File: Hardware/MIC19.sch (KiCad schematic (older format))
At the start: 14 parts, among them J001 ENGINE_VEL, J002 ENGINE_ACEL, J003 MPPT_POT, J004 SW_PUMP1_ON, J005 SW_PUMP2_ON, J006 SW_PUMP3_ON, J007 SW_BOAT_ON, J008 SW_ENGINE_ON, J009 SW_MPPT_ON, J010 SW_DMS

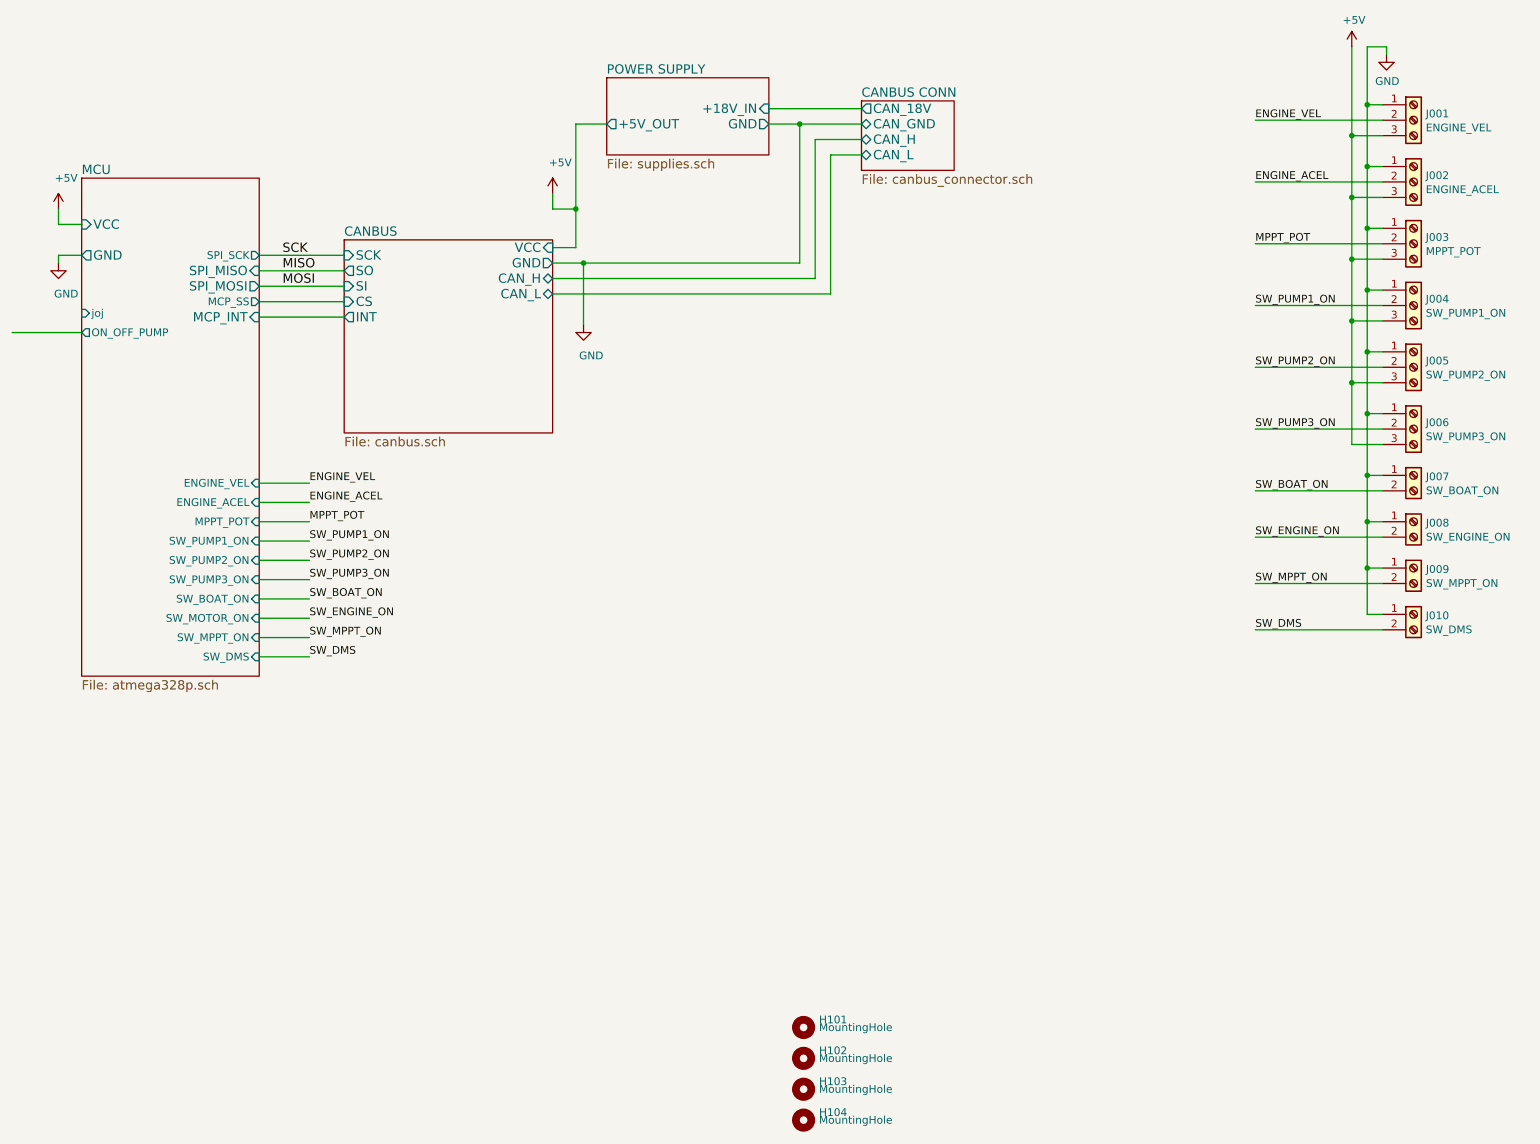
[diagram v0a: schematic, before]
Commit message: Atualização do MIC19
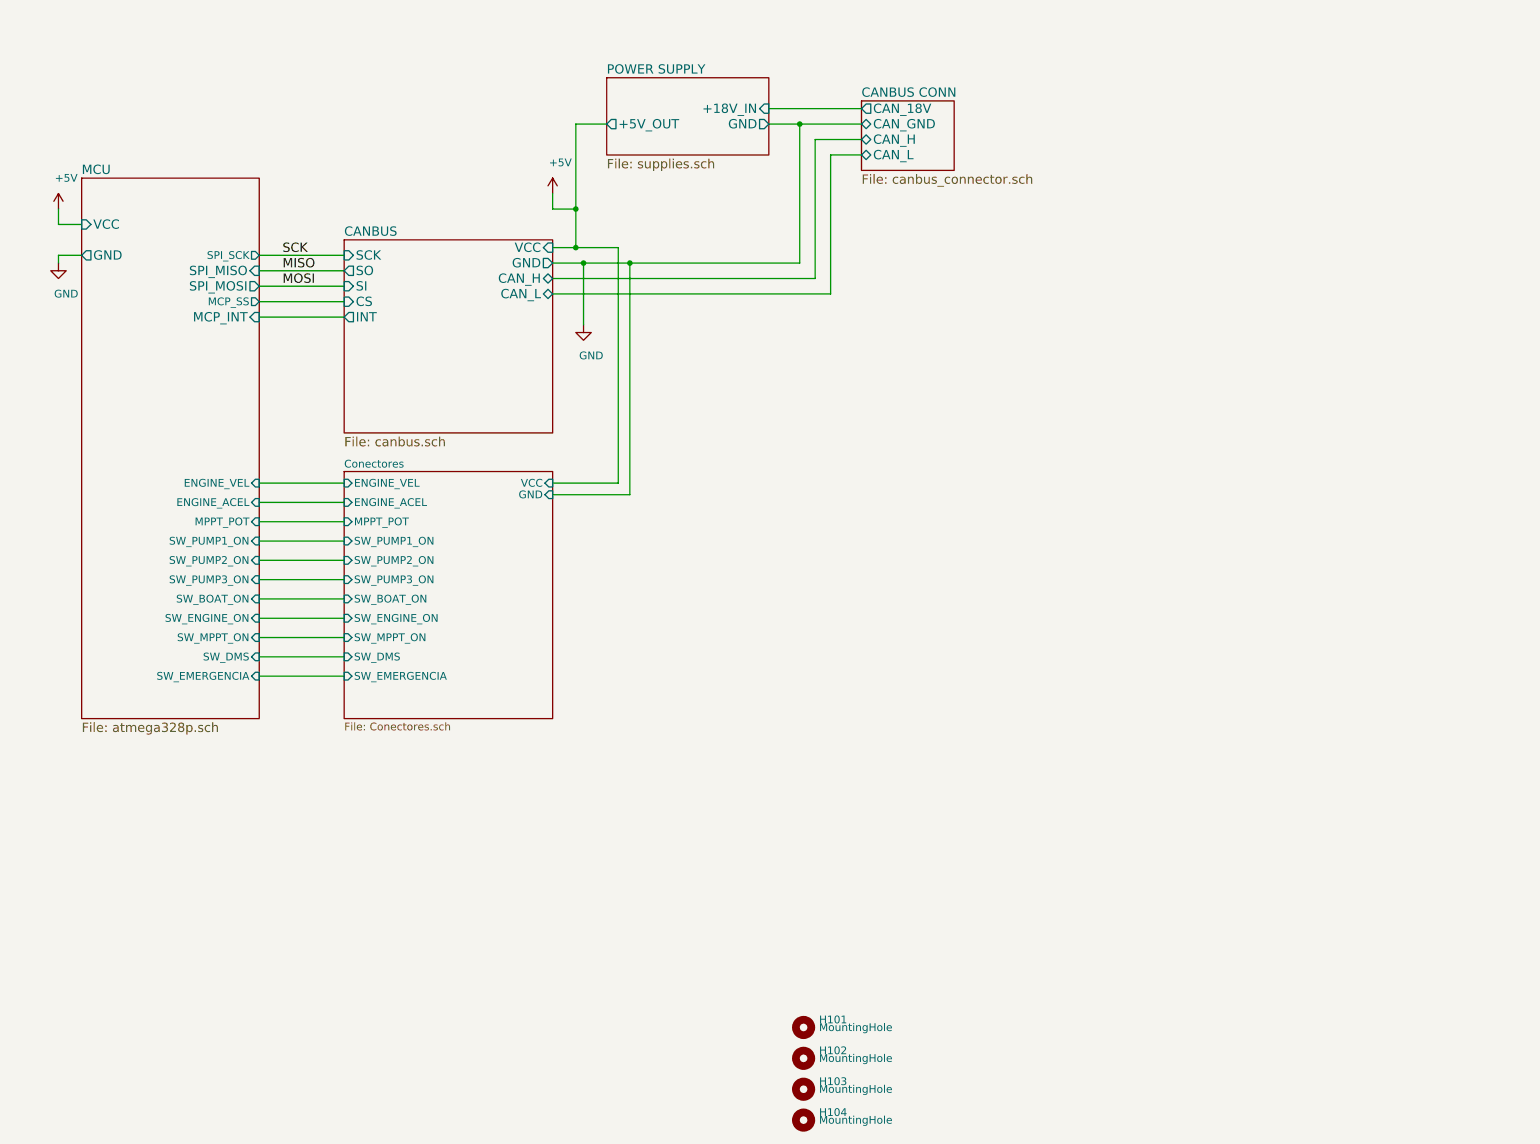
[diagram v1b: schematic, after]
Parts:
- removed J001: ENGINE_VEL, symbol Connector:Screw_Terminal_01x03
- removed J002: ENGINE_ACEL, symbol Connector:Screw_Terminal_01x03
- removed J003: MPPT_POT, symbol Connector:Screw_Terminal_01x03
- removed J004: SW_PUMP1_ON, symbol Connector:Screw_Terminal_01x03
- removed J005: SW_PUMP2_ON, symbol Connector:Screw_Terminal_01x03
- removed J006: SW_PUMP3_ON, symbol Connector:Screw_Terminal_01x03
- removed J007: SW_BOAT_ON, symbol Connector:Screw_Terminal_01x02
- removed J008: SW_ENGINE_ON, symbol Connector:Screw_Terminal_01x02
- removed J009: SW_MPPT_ON, symbol Connector:Screw_Terminal_01x02
- removed J010: SW_DMS, symbol Connector:Screw_Terminal_01x02
